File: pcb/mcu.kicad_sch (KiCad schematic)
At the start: 24 parts, among them J1 3220-10-0100-00, J2 Conn_01x03_Pin, J3 Conn_01x03_Pin, SW1 PTS815, U1 STM32F446RETx, Y1 ECS-160-12-33B2Q-JES-TR3

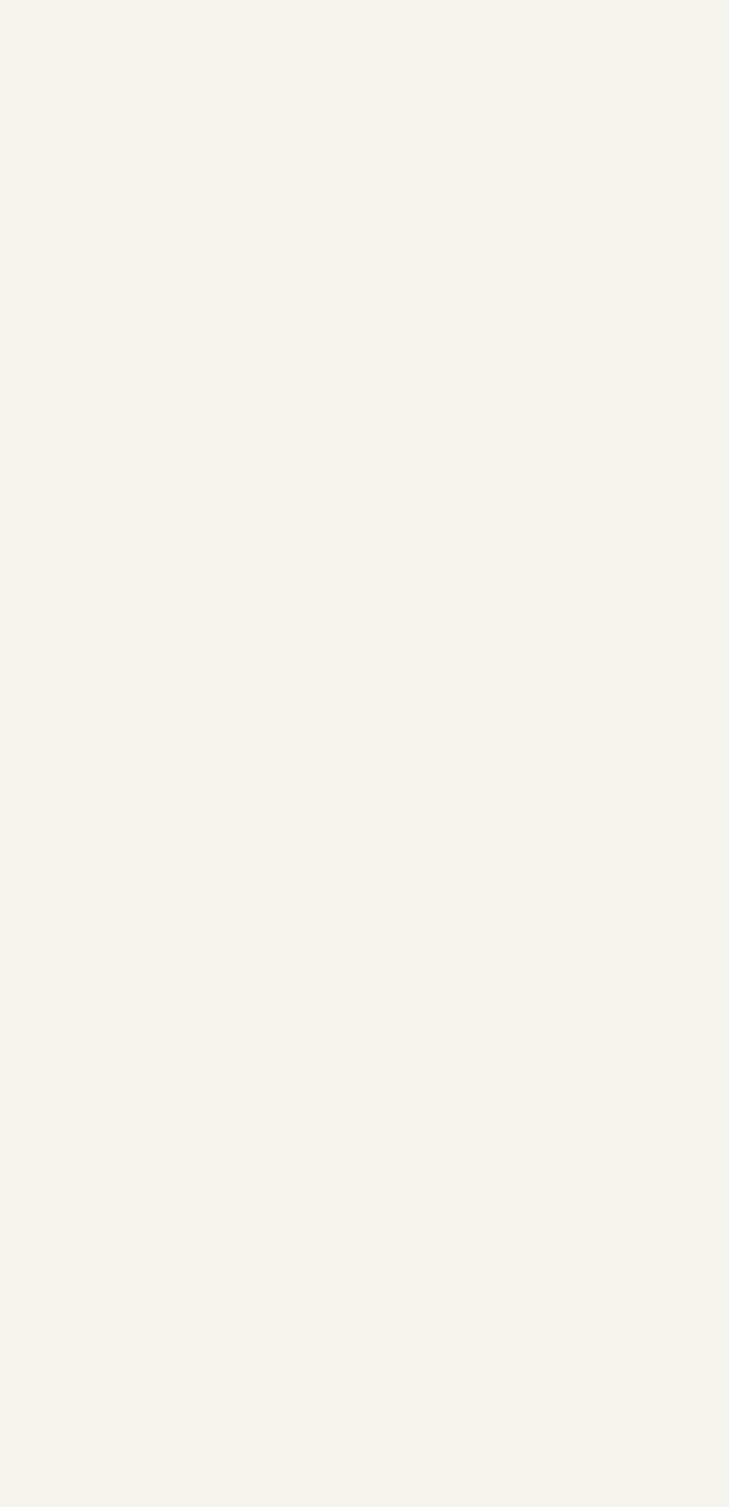
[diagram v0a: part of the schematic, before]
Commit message: Add stm32h523vetx to schematic
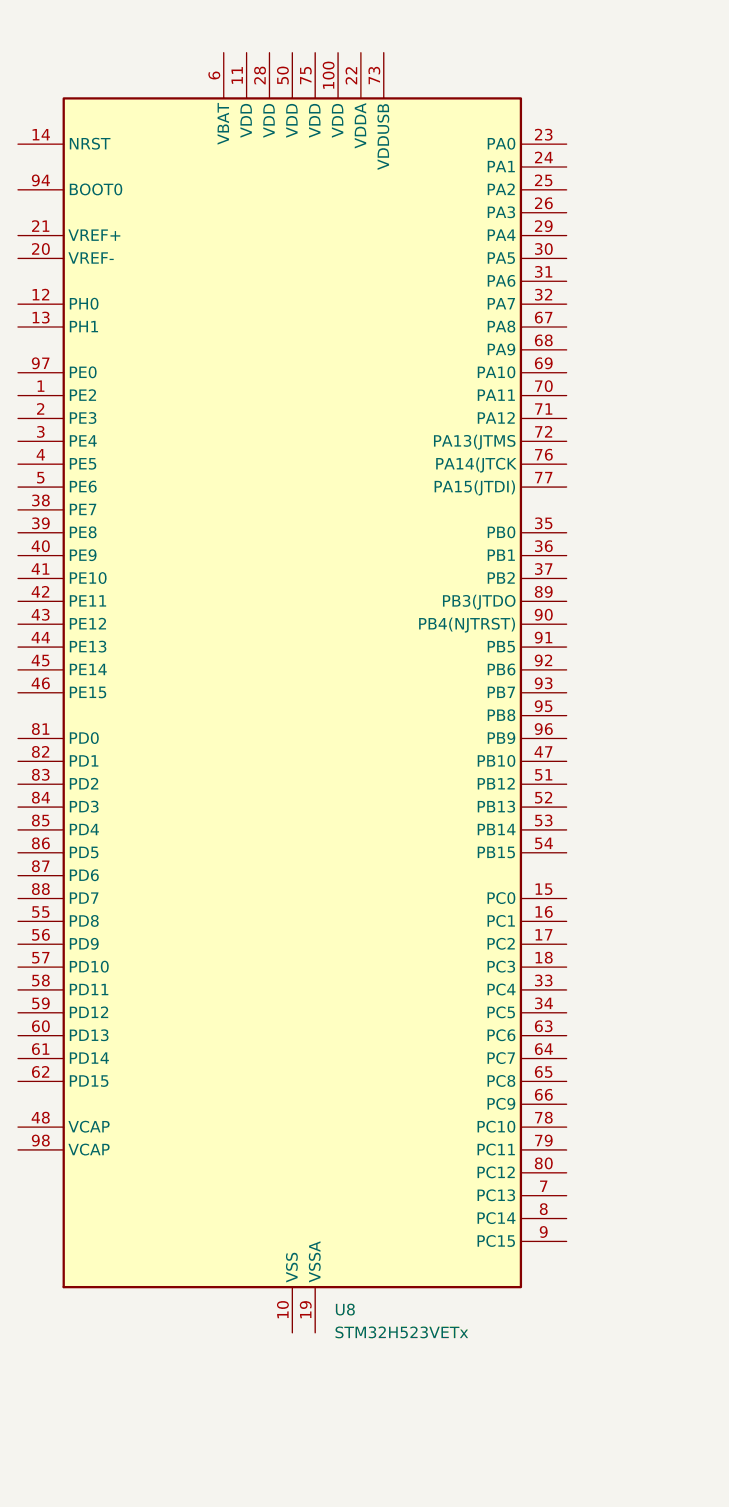
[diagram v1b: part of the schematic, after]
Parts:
- added U8: STM32H523VETx, Package_QFP:LQFP-100_14x14mm_P0.5mm, symbol MCU_ST_STM32H5:STM32H523VETx
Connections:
- new net: U8.10 (VSS), U8.27 (VSS), U8.49 (VSS), U8.74 (VSS), U8.99 (VSS)

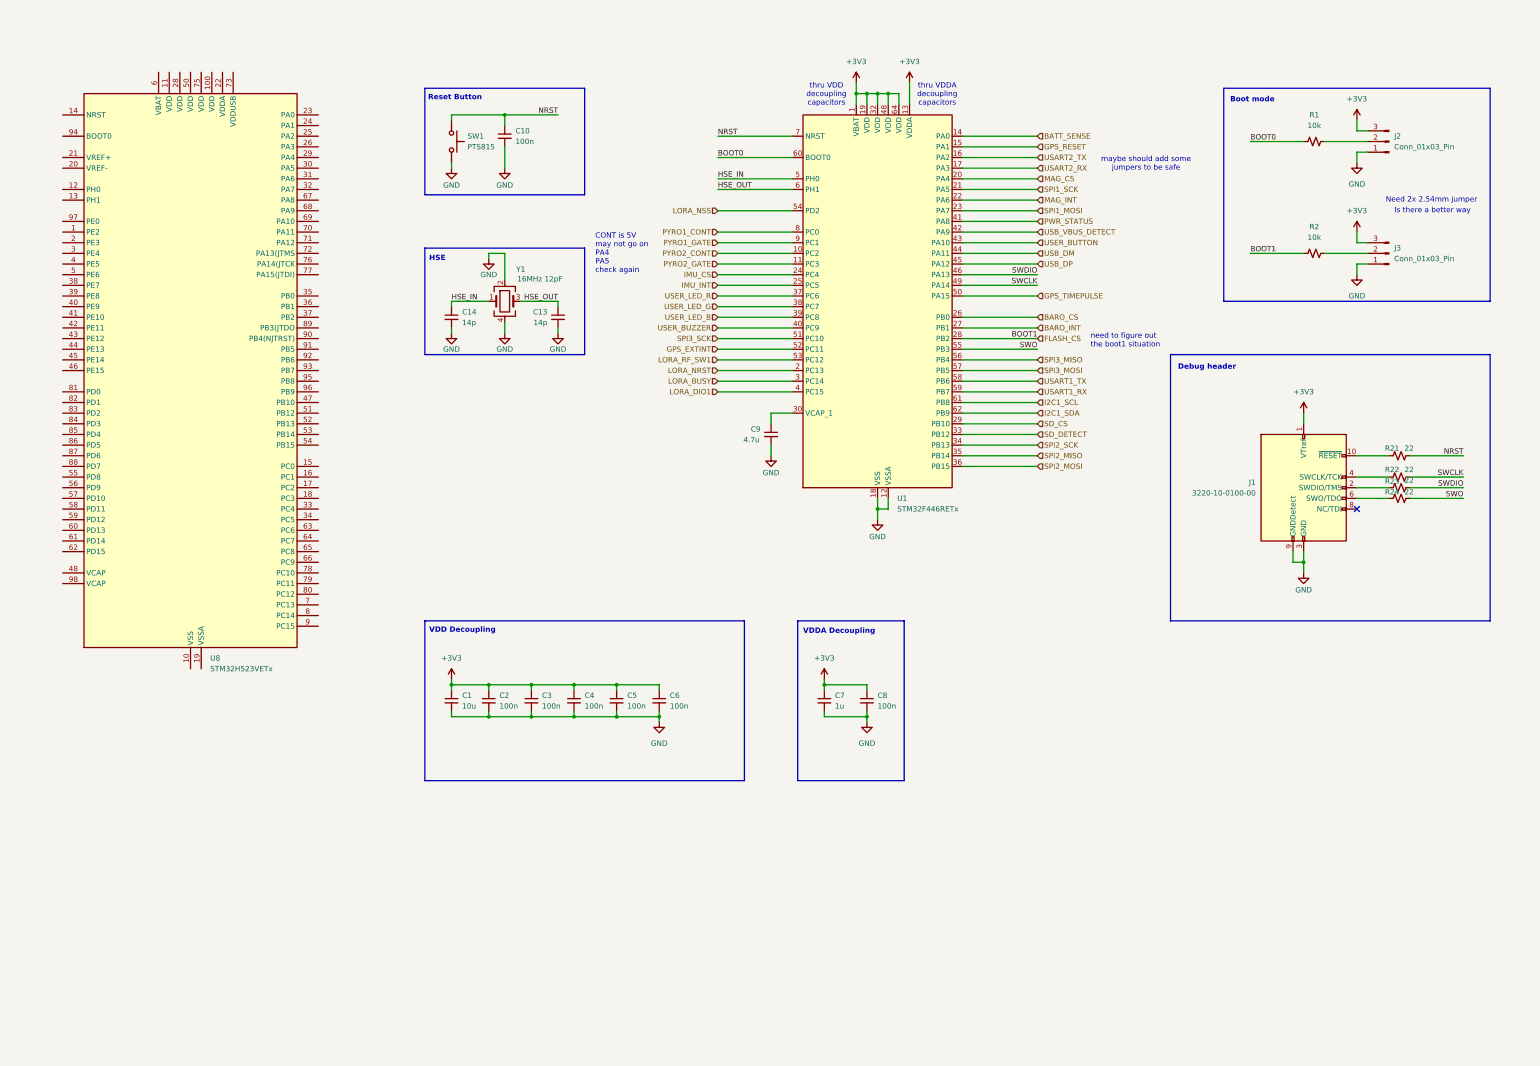
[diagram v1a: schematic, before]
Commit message: Improve inter sheet connections
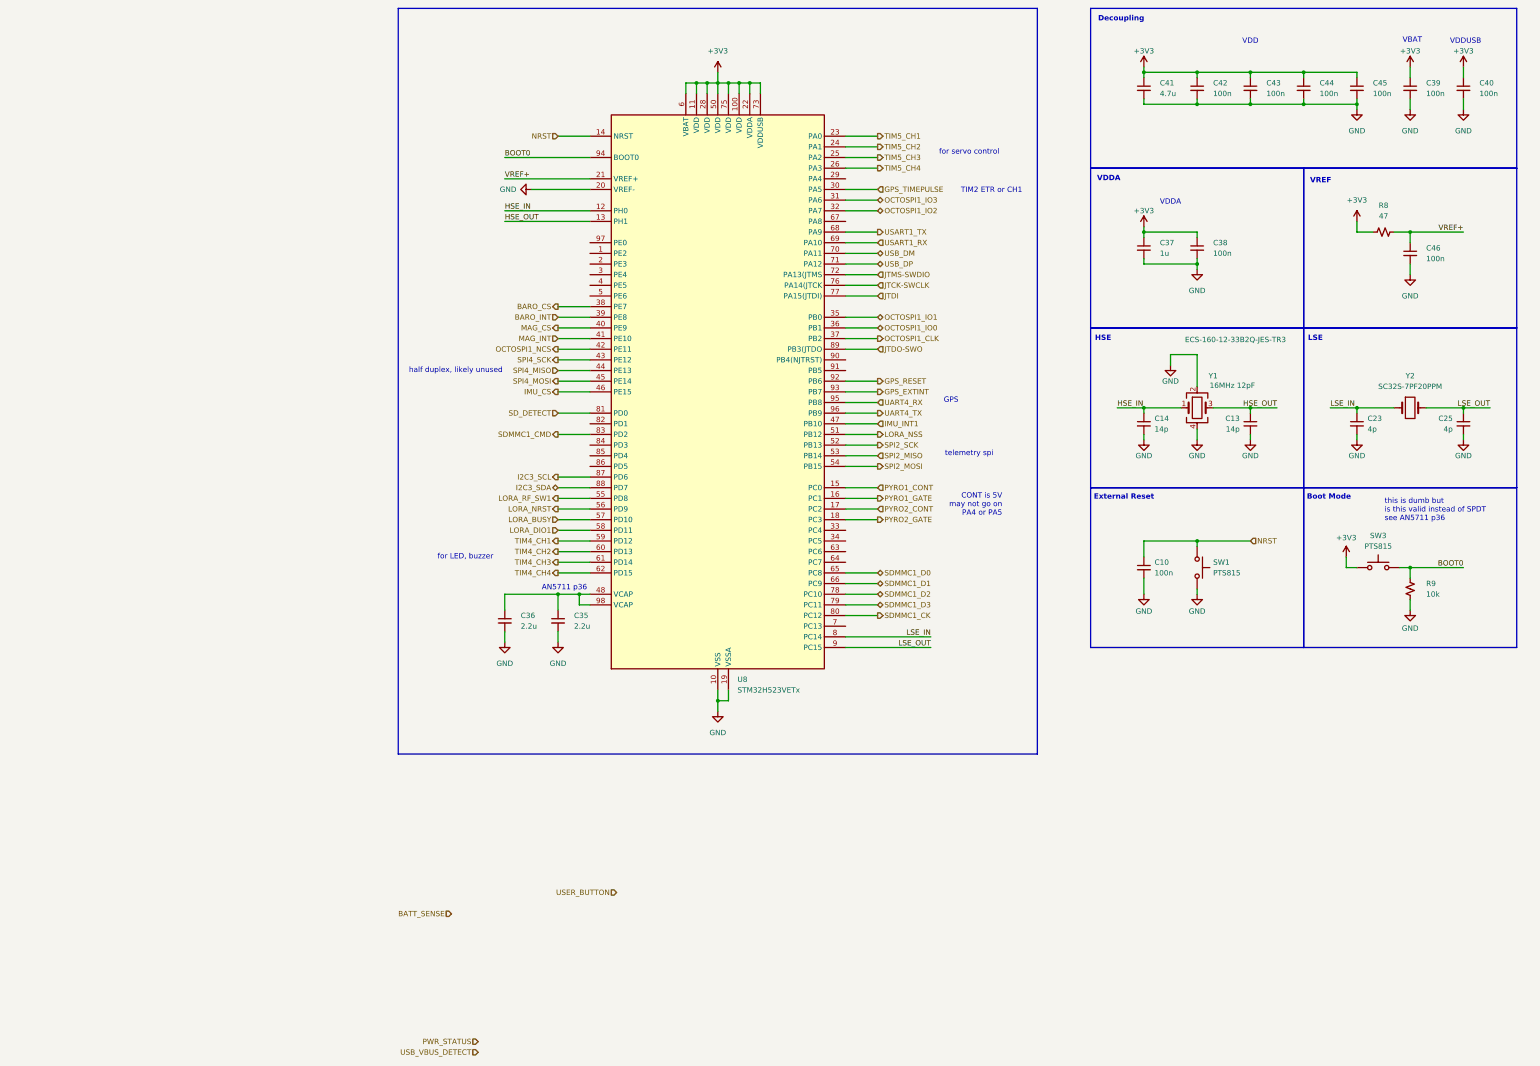
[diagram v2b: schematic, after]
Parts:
- removed C1: 10u, symbol Device:C_Small
- removed C2, C3, C4, C5, C6, C8: 100n, symbol Device:C_Small
- removed C7: 1u, symbol Device:C_Small
- removed C9: 4.7u, symbol Device:C_Small
- removed J1: 3220-10-0100-00, symbol Connector:Conn_ARM_JTAG_SWD_10
- removed J2, J3: Conn_01x03_Pin, symbol Connector:Conn_01x03_Pin
- removed R1, R2: 10k, symbol Device:R_Small_US
- removed R21, R22, R23, R24: 22, symbol Device:R_Small_US
- removed U1: STM32F446RETx, Package_QFP:LQFP-64_10x10mm_P0.5mm, symbol MCU_ST_STM32F4:STM32F446RETx
- added C23, C25: 4p, symbol Device:C_Small
- added C35, C36: 2.2u, symbol Device:C_Small
- added C37: 1u, symbol Device:C_Small
- added C38, C39, C40, C42, C43, C44, C45, C46: 100n, symbol Device:C_Small
- added C41: 4.7u, symbol Device:C_Small
- added R8: 47, symbol Device:R_Small_US
- added R9: 10k, symbol Device:R_Small_US
- added SW3: PTS815, symbol Switch:SW_Push
- added Y2: SC32S-7PF20PPM, symbol Device:Crystal
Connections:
- net +3V3: now also U8.100 (VDD), U8.11 (VDD), U8.22 (VDDA), U8.28 (VDD), U8.50 (VDD), U8.6 (VBAT), U8.73 (VDDUSB), U8.75 (VDD), C37.1, C38.1, C39.1, C40.1, C41.1, C42.1, C43.1, C44.1, C45.1, R8.1, SW3.1
- net BARO_CS: now also U8.38 (PE7)
- net BARO_INT: now also U8.39 (PE8)
- net BOOT0: now also U8.94 (BOOT0), R9.1, SW3.2
- net GND: now also U8.10 (VSS), U8.19 (VSSA), U8.20 (VREF-), U8.27 (VSS), U8.49 (VSS), U8.74 (VSS), U8.99 (VSS), C23.2, C25.2, C35.2, C36.2, C37.2, C38.2, C39.2, C40.2, C41.2, C42.2, C43.2, C44.2, C45.2, C46.2, R9.2
- net GPS_EXTINT: now also U8.93 (PB7)
- net GPS_RESET: now also U8.92 (PB6)
- net GPS_TIMEPULSE: now also U8.30 (PA5)
- net HSE_IN: now also U8.12 (PH0)
- net HSE_OUT: now also U8.13 (PH1)
- net IMU_CS: now also U8.46 (PE15)
- net LORA_BUSY: now also U8.57 (PD10)
- net LORA_DIO1: now also U8.58 (PD11)
- net LORA_NRST: now also U8.56 (PD9)
- net LORA_NSS: now also U8.51 (PB12)
- net LORA_RF_SW1: now also U8.55 (PD8)
- net MAG_CS: now also U8.40 (PE9)
- net MAG_INT: now also U8.41 (PE10)
- net NRST: now also U8.14 (NRST)
- net PYRO1_CONT: now also U8.15 (PC0)
- net PYRO1_GATE: now also U8.16 (PC1)
- net PYRO2_CONT: now also U8.17 (PC2)
- net PYRO2_GATE: now also U8.18 (PC3)
- net SD_DETECT: now also U8.81 (PD0)
- net SPI2_MISO: now also U8.53 (PB14)
- net SPI2_MOSI: now also U8.54 (PB15)
- net SPI2_SCK: now also U8.52 (PB13)
- net USART1_RX: now also U8.69 (PA10)
- net USART1_TX: now also U8.68 (PA9)
- net USB_DM: now also U8.70 (PA11)
- net USB_DP: now also U8.71 (PA12)
- net VREF+: now reaches U8.21 (VREF+)
- net VREF+: now also C46.1, R8.2
- net TIM5_CH1: now reaches U8.23 (PA0)
- net TIM5_CH2: now reaches U8.24 (PA1)
- net TIM5_CH3: now reaches U8.25 (PA2)
- net TIM5_CH4: now reaches U8.26 (PA3)
- net OCTOSPI1_IO3: now reaches U8.31 (PA6)
- net OCTOSPI1_IO2: now reaches U8.32 (PA7)
- net OCTOSPI1_IO1: now reaches U8.35 (PB0)
- net OCTOSPI1_IO0: now reaches U8.36 (PB1)
- net OCTOSPI1_CLK: now reaches U8.37 (PB2)
- net OCTOSPI1_NCS: now reaches U8.42 (PE11)
- net SPI4_SCK: now reaches U8.43 (PE12)
- net SPI4_MISO: now reaches U8.44 (PE13)
- net SPI4_MOSI: now reaches U8.45 (PE14)
- net IMU_INT1: now reaches U8.47 (PB10)
- net at U8.48 (VCAP): now also U8.98 (VCAP), C35.1, C36.1
- net TIM4_CH1: now reaches U8.59 (PD12)
- net TIM4_CH2: now reaches U8.60 (PD13)
- net TIM4_CH3: now reaches U8.61 (PD14)
- net TIM4_CH4: now reaches U8.62 (PD15)
- net SDMMC1_D0: now reaches U8.65 (PC8)
- net SDMMC1_D1: now reaches U8.66 (PC9)
- net JTMS-SWDIO: now reaches U8.72 (PA13(JTMS)
- net JTCK-SWCLK: now reaches U8.76 (PA14(JTCK)
- net JTDI: now reaches U8.77 (PA15(JTDI))
- net SDMMC1_D2: now reaches U8.78 (PC10)
- net SDMMC1_D3: now reaches U8.79 (PC11)
- net LSE_IN: now reaches U8.8 (PC14)
- net LSE_IN: now also C23.1, Y2.1
- net SDMMC1_CK: now reaches U8.80 (PC12)
- net SDMMC1_CMD: now reaches U8.83 (PD2)
- net I2C3_SCL: now reaches U8.87 (PD6)
- net I2C3_SDA: now reaches U8.88 (PD7)
- net JTDO-SWO: now reaches U8.89 (PB3(JTDO)
- net LSE_OUT: now reaches U8.9 (PC15)
- net LSE_OUT: now also C25.1, Y2.2
- net UART4_RX: now reaches U8.95 (PB8)
- net UART4_TX: now reaches U8.96 (PB9)
- no-connect marks 1 -> 0
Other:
- note added: "AN5711 p36"
- note added: "Boot Mode"
- note added: "CONT is 5V may not go on PA4 or PA5"
- note added: "Decoupling"
- note added: "External Reset"
- note added: "GPS"
- note added: "LSE"
- note added: "TIM2 ETR or CH1"
- note added: "VBAT"
- note added: "VDD"
- note added: "VDDA"
- note added: "VDDUSB"
- note added: "VREF"
- note added: "for LED, buzzer"
- note added: "for servo control"
- note added: "half duplex, likely unused"
- note added: "telemetry spi"
- note added: "this is dumb but is this valid instead of SPDT see AN5711 p36"
- note removed: "Boot mode"
- note removed: "CONT is 5V may not go on PA4 PA5 check again"
- note removed: "Debug header"
- note removed: "Is there a better way"
- note removed: "Need 2x 2.54mm jumper"
- note removed: "Reset Button"
- note removed: "VDD Decoupling"
- note removed: "VDDA Decoupling"
- note removed: "maybe should add some jumpers to be safe"
- note removed: "need to figure out the boot1 situation"
- note removed: "thru VDD decoupling capacitors"
- note removed: "thru VDDA decoupling capacitors"
- title: (none) -> Flight Computer
- moved on the sheet: C10, C13, C14, SW1, U8, Y1
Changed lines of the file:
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@@
 	(generator_version "9.0")
 	(paper "A4")
+	(title_block
+		(title "Flight Computer")
+	)
